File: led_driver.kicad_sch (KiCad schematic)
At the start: 33 parts, among them J1 BarrelJack_3167288, J2 USB4105-GF-A, U1 MP2483DQ-LF-P, U2 AP62301Z6-7

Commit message: Refresh standardization on schematic and PCB
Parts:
- C10, C11: Author (none) -> Antmicro; Copyright Copyright (c) 2023 Antmicro -> (none); License Apache-2.0 License -> Apache-2.0; Manufacturer MURATA -> Murata
- C12, C13, C3, C6, C7, C8, C9, J1, R12, R13, R14, R4, R6, R9: Author (none) -> Antmicro; Copyright Copyright (c) 2023 Antmicro -> (none); License Apache-2.0 License -> Apache-2.0
- C2: footprint antmicro-footprints:0603-cap -> antmicro-footprints:C_0603_1608Metric; Author (none) -> Antmicro; Copyright Copyright (c) 2023 Antmicro -> (none); License Apache-2.0 License -> Apache-2.0
- C4, C5: footprint antmicro-footprints:0402-cap -> antmicro-footprints:C_0402_1005Metric; Author (none) -> Antmicro; Copyright Copyright (c) 2023 Antmicro -> (none); License Apache-2.0 License -> Apache-2.0; Manufacturer WURTH_ELEKTRONIK -> Würth Elektronik
- D1: Author (none) -> Antmicro; License (none) -> Apache-2.0
- J2: value USB4105-GF-A -> USB-C_USB4105-GF-A; symbol antmicroUSBDVIHDMIConnectors:USB4105-GF-A -> antmicroUSBDVIHDMIConnectors:USB-C_USB4105-GF-A; Author (none) -> Antmicro; License (none) -> Apache-2.0
- L2: symbol antmicroFixedInductors:TFM252012ALMA3R3MTAA -> antmicroFixedInductors:L_3u3_2.1A_1008; Author (none) -> Antmicro; IMax (none) -> 2.5; ISat (none) -> 2.1; License (none) -> Apache-2.0; VAL 3.3uH/2.1A -> (none); Val (none) -> 3.3u/2.1A
- POT1: value R0141-2-20k -> POT_20k_R0141-2-20k; footprint antmicro-footprints:Potentiometer_SRPassives_R0141-2_Horizontal -> antmicro-footprints:POT_R0141-2; symbol antmicroRotaryPotentiometersRheostats:R0141-2-20k -> antmicroRotaryPotentiometersRheostats:POT_20k_R0141-2-20k; Author (none) -> Antmicro
- R1: footprint antmicro-footprints:1206-res -> antmicro-footprints:R_1206_3216Metric; Author (none) -> Antmicro; Copyright Copyright (c) 2023 Antmicro -> (none); License Apache-2.0 License -> Apache-2.0
- R2, R3, R8: footprint antmicro-footprints:0402-res -> antmicro-footprints:R_0402_1005Metric; Author (none) -> Antmicro; Copyright Copyright (c) 2023 Antmicro -> (none); License Apache-2.0 License -> Apache-2.0
- R5: footprint antmicro-footprints:0603-res -> antmicro-footprints:R_0603_1608Metric; Author (none) -> Antmicro; Copyright Copyright (c) 2023 Antmicro -> (none); License Apache-2.0 License -> Apache-2.0
- TP1: footprint antmicro-footprints:TP_SMD_1_MM -> antmicro-footprints:Testpoint_smd_1mm; Author (none) -> Antmicro; Copyright Copyright (c) 2023 Antmicro -> (none); License Apache-2.0 License -> Apache-2.0
- U1: footprint antmicro-footprints:MP2483DQ-LF-P -> antmicro-footprints:QFN-10-1EP_3x3mm_P0.5mm; symbol antmicroPMICLEDDrivers:MP2483DQ-LF-P -> antmicroPMICLEDDrivers:MP2483D_QFN; Author (none) -> Antmicro; License (none) -> Apache-2.0; Manufacturer Monolithic Power Systems Inc. -> Monolithic Power Systems
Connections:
- net GND: now also J2.SH (SHIELD), U1.11 (EP); no longer J2.S1 (SHIELD), U1.EPAD
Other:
- moved on the sheet: C12, C13, C2, C3, C4, C5, C7, C8, C9, D1, L1, R1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

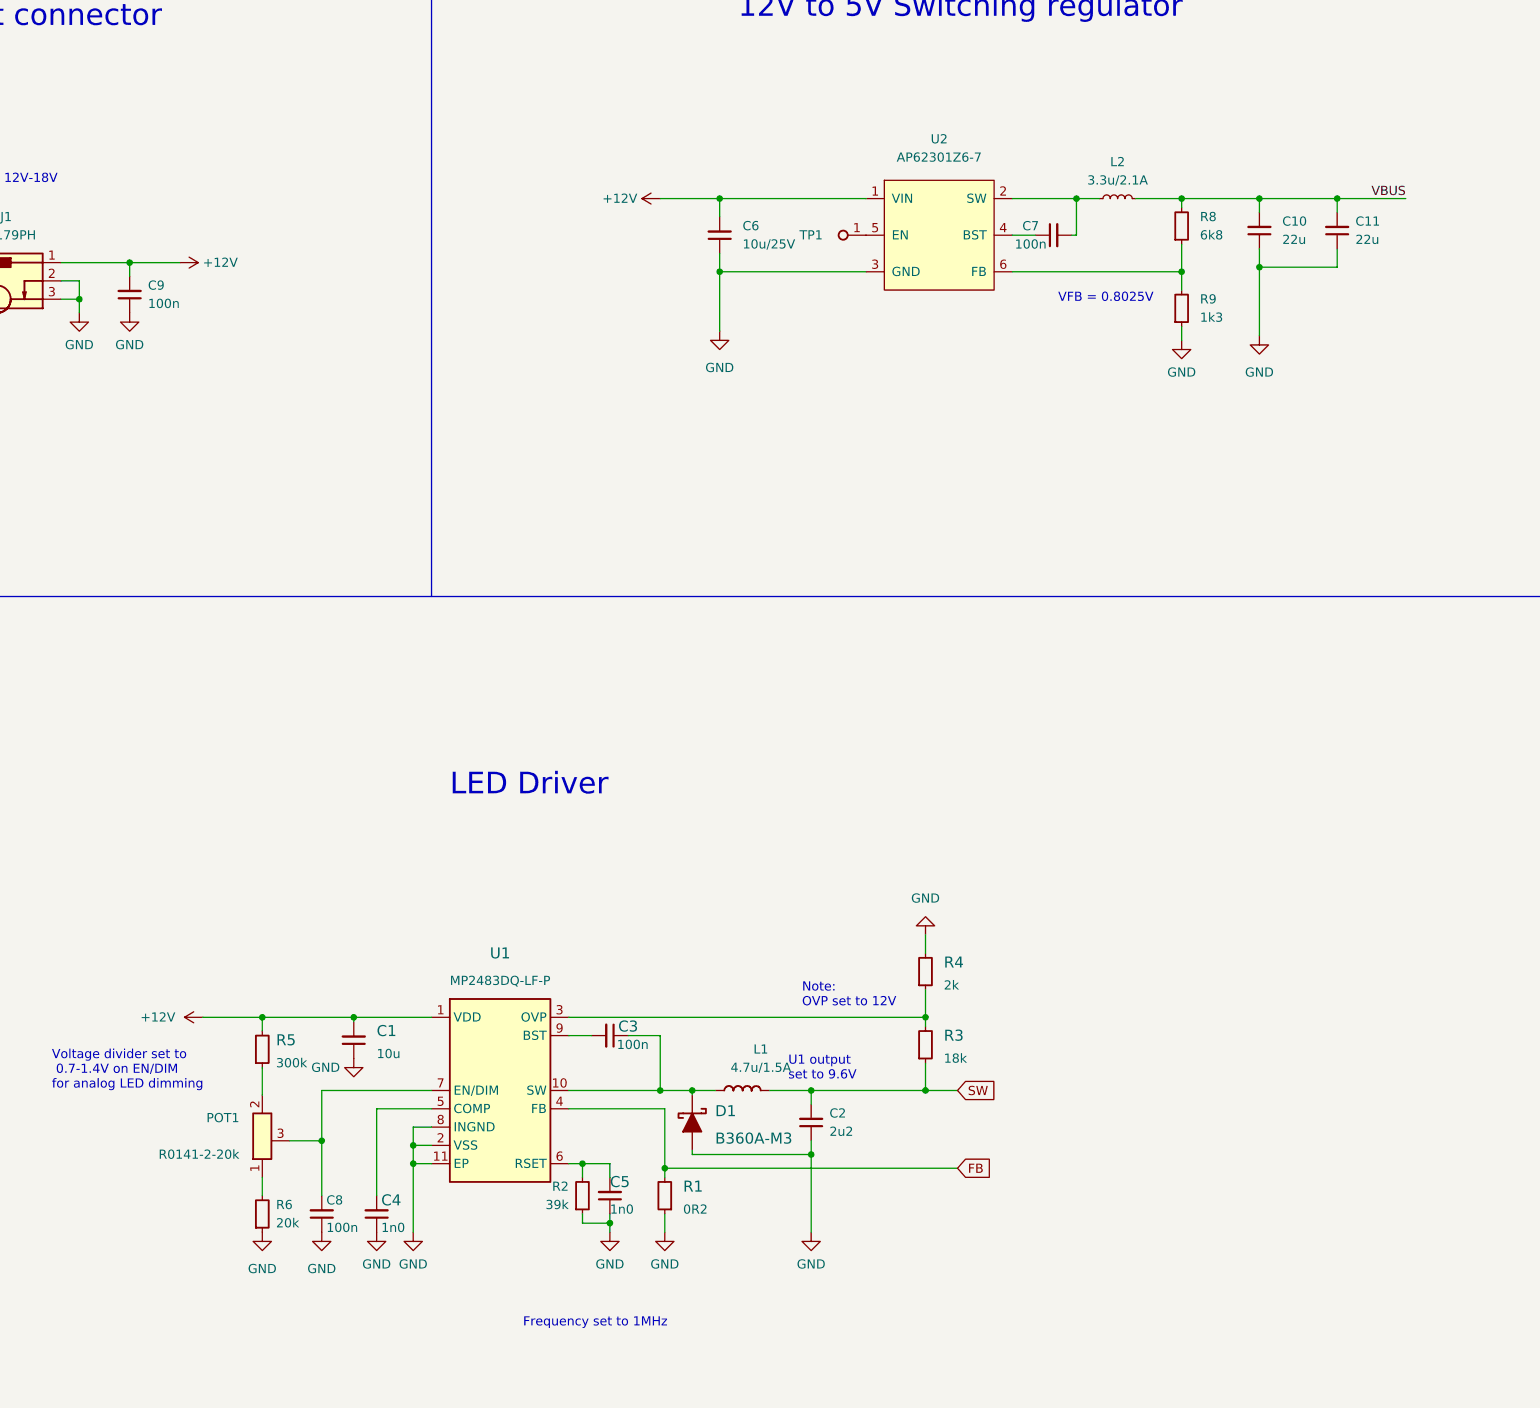
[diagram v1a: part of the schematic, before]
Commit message: Introduced schematic standardization
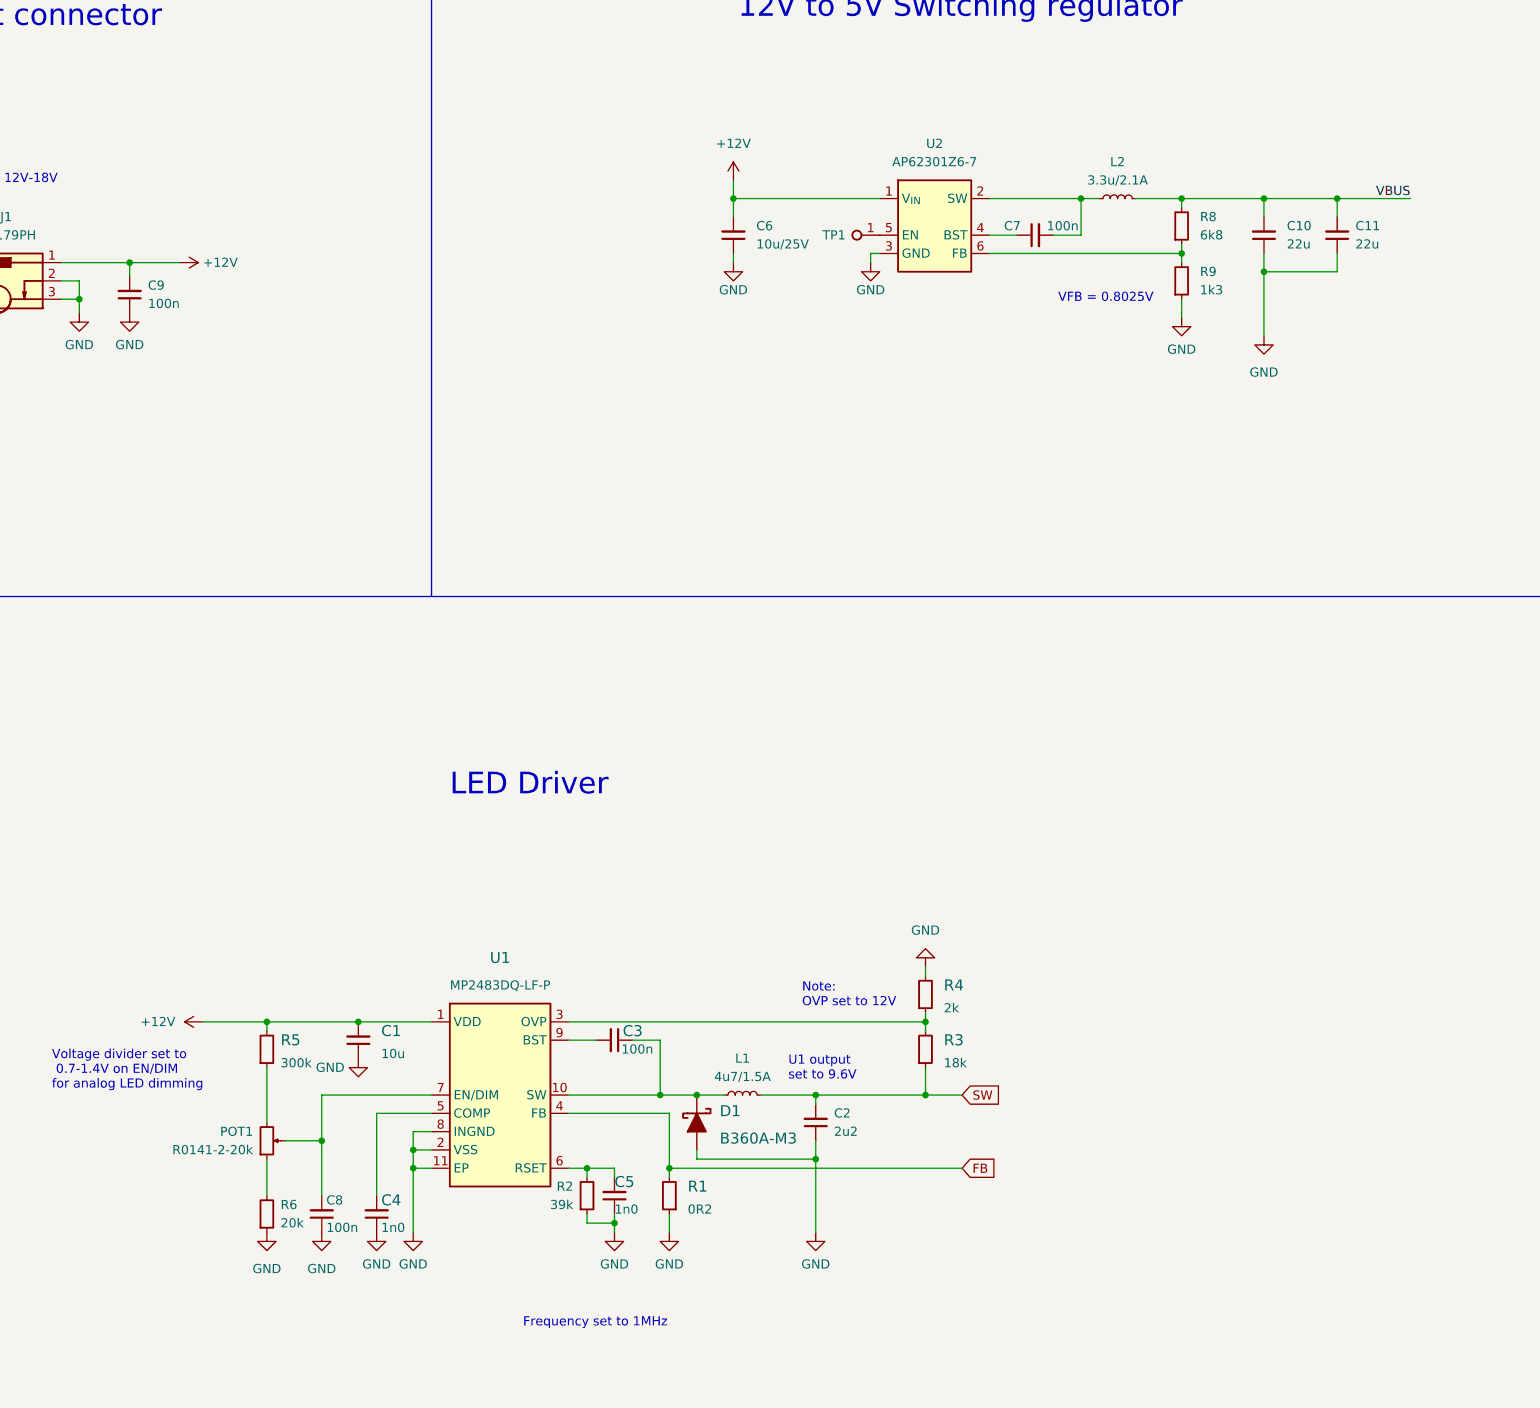
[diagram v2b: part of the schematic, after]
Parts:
- removed L1: SRP2512A-4R7M, antmicro-footprints:SRP2512A-1R0M, symbol antmicroFixedInductors:SRP2512A-4R7M
- added L1: L_4u7_1.5A_1008, antmicro-footprints:SRP2512A-1R0M, symbol antmicroFixedInductors:L_4u7_1.5A_1008
- C1: footprint antmicro-footprints:0805-cap -> antmicro-footprints:C_0805_2012Metric; Author (none) -> Antmicro; License Apache-2.0 License -> Apache-2.0; Manufacturer JOHANSON_DIELECTRICS -> Johanson Technology Inc.
- J2: footprint antmicro-footprints:GCT_USB4105-GF-A -> antmicro-footprints:USB-C_GCT_USB4105-GF-A
- U2: Author (none) -> Antmicro; License (none) -> Apache-2.0
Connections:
- net SW: now also L1.2
- net at C3.1, D1.K, U1.10 (SW): now also L1.1
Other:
- company: (none) -> Antmicro Ltd.
- moved on the sheet: C1, C10, C11, C2, C3, C5, C6, C7, D1, R1, R2, R3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

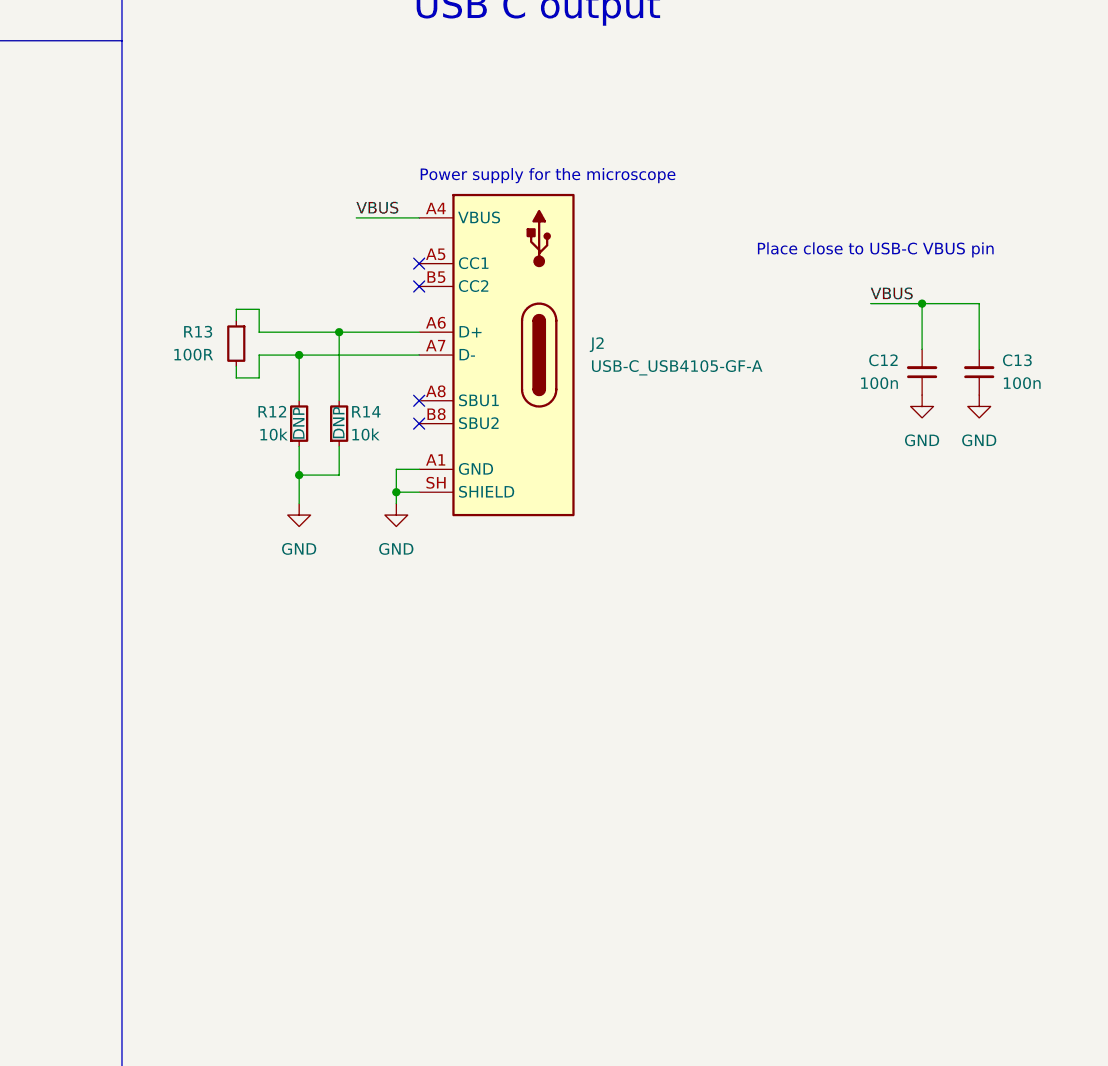
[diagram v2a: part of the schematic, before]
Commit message: [50954] Added CC resistors and OHP assets, updated README
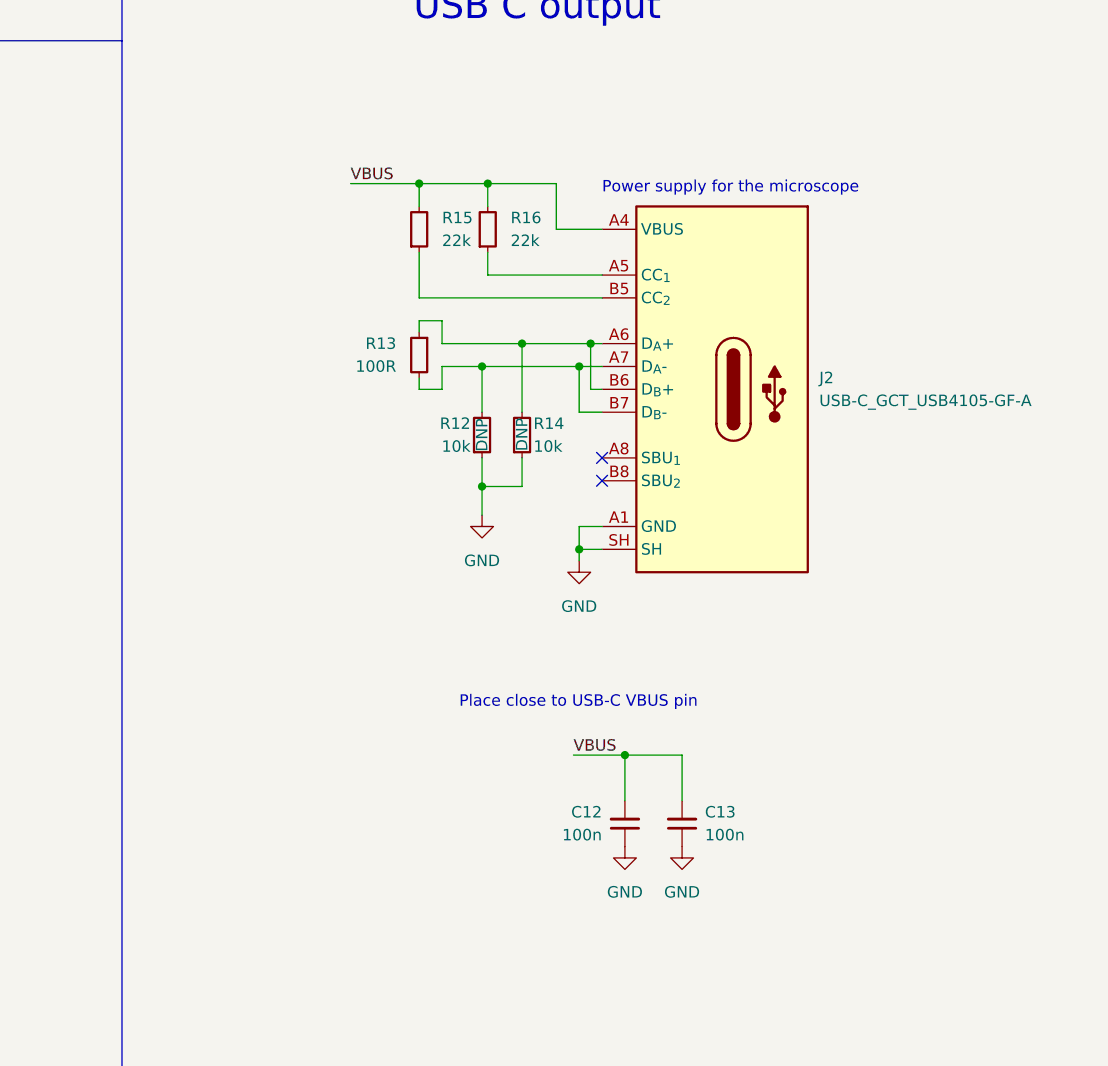
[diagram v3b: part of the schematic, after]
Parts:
- removed J2: USB-C_USB4105-GF-A, antmicro-footprints:USB-C_GCT_USB4105-GF-A, symbol antmicroUSBDVIHDMIConnectors:USB-C_USB4105-GF-A
- added J2: USB-C_GCT_USB4105-GF-A, antmicro-footprints:USB-C_Receptacle_GCT_USB4105-GF-A, symbol antmicroUSBConnectors:USB-C_GCT_USB4105-GF-A
- added R15, R16: R_22k_0402, antmicro-footprints:R_0402_1005Metric, symbol antmicroResistors0402:R_22k_0402
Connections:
- net GND: now also J2.A1 (GND), J2.A12 (GND), J2.B1 (GND), J2.B12 (GND), J2.SH
- net VBUS: now also J2.A4 (VBUS), J2.A9 (VBUS), J2.B4 (VBUS), J2.B9 (VBUS), R15.2, R16.2
- net at R13.1, R14.2: now also J2.A6 (D_{A}+), J2.B6 (D_{B}+)
- net at R12.2, R13.2: now also J2.A7 (D_{A}-), J2.B7 (D_{B}-)
- new net: J2.A5 (CC_{1}), R16.1
- new net: J2.B5 (CC_{2}), R15.1
- no-connect marks 4 -> 2
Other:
- moved on the sheet: C12, C13, R12, R13, R14
